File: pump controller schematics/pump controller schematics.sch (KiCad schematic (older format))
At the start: 16 parts, among them J1 Barrel_Jack, M1 370 pump, Q1 IRF64ON, SW1 SW_DIP_x01, U1 LM555

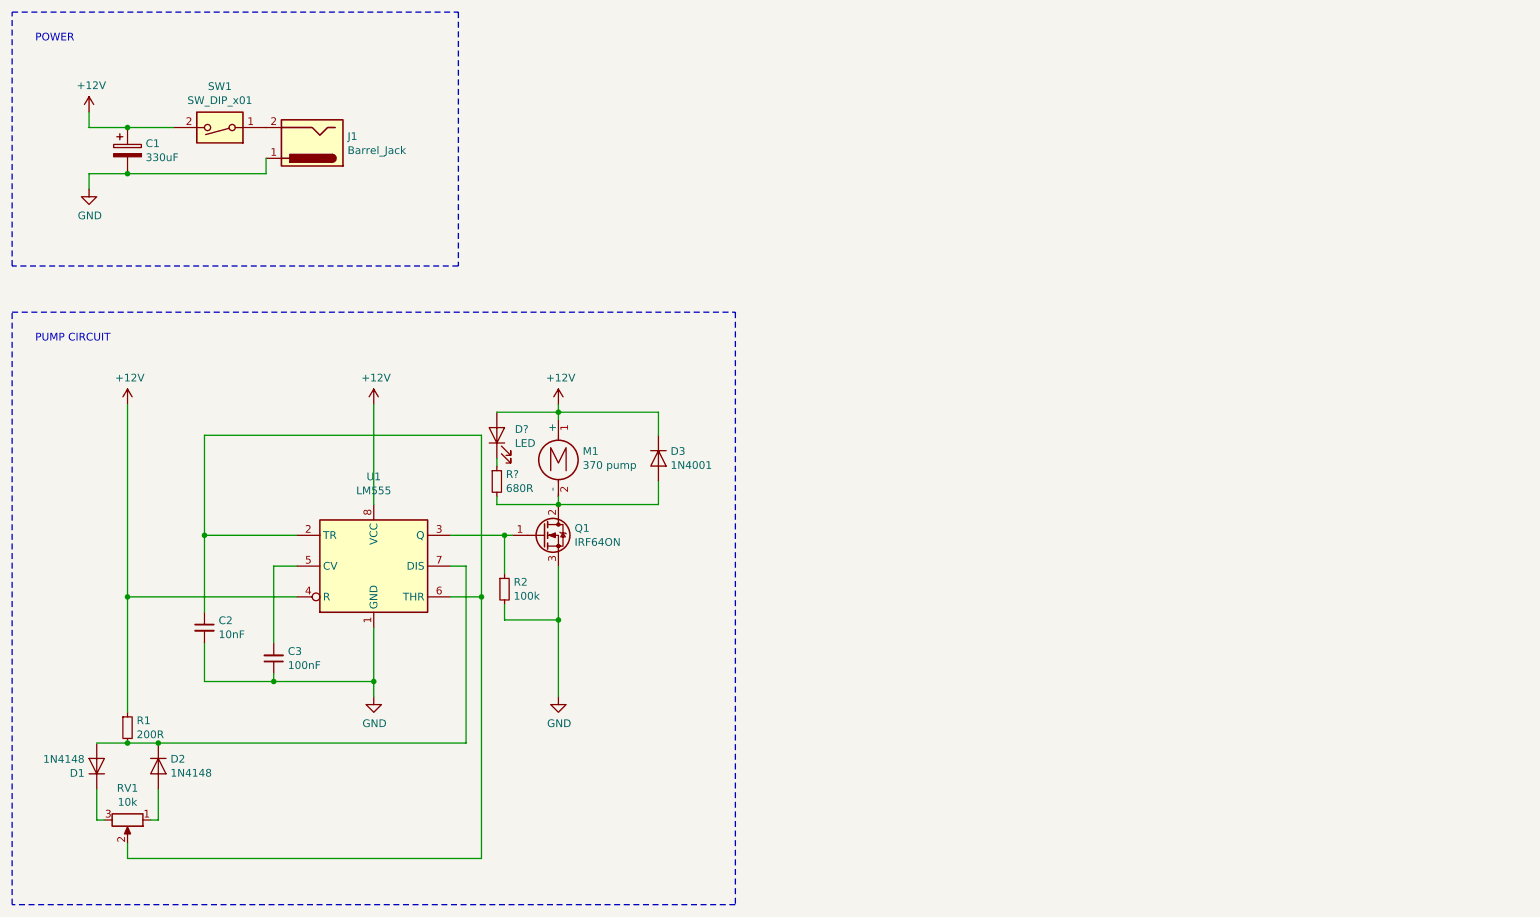
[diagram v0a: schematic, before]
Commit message: updated pump controller
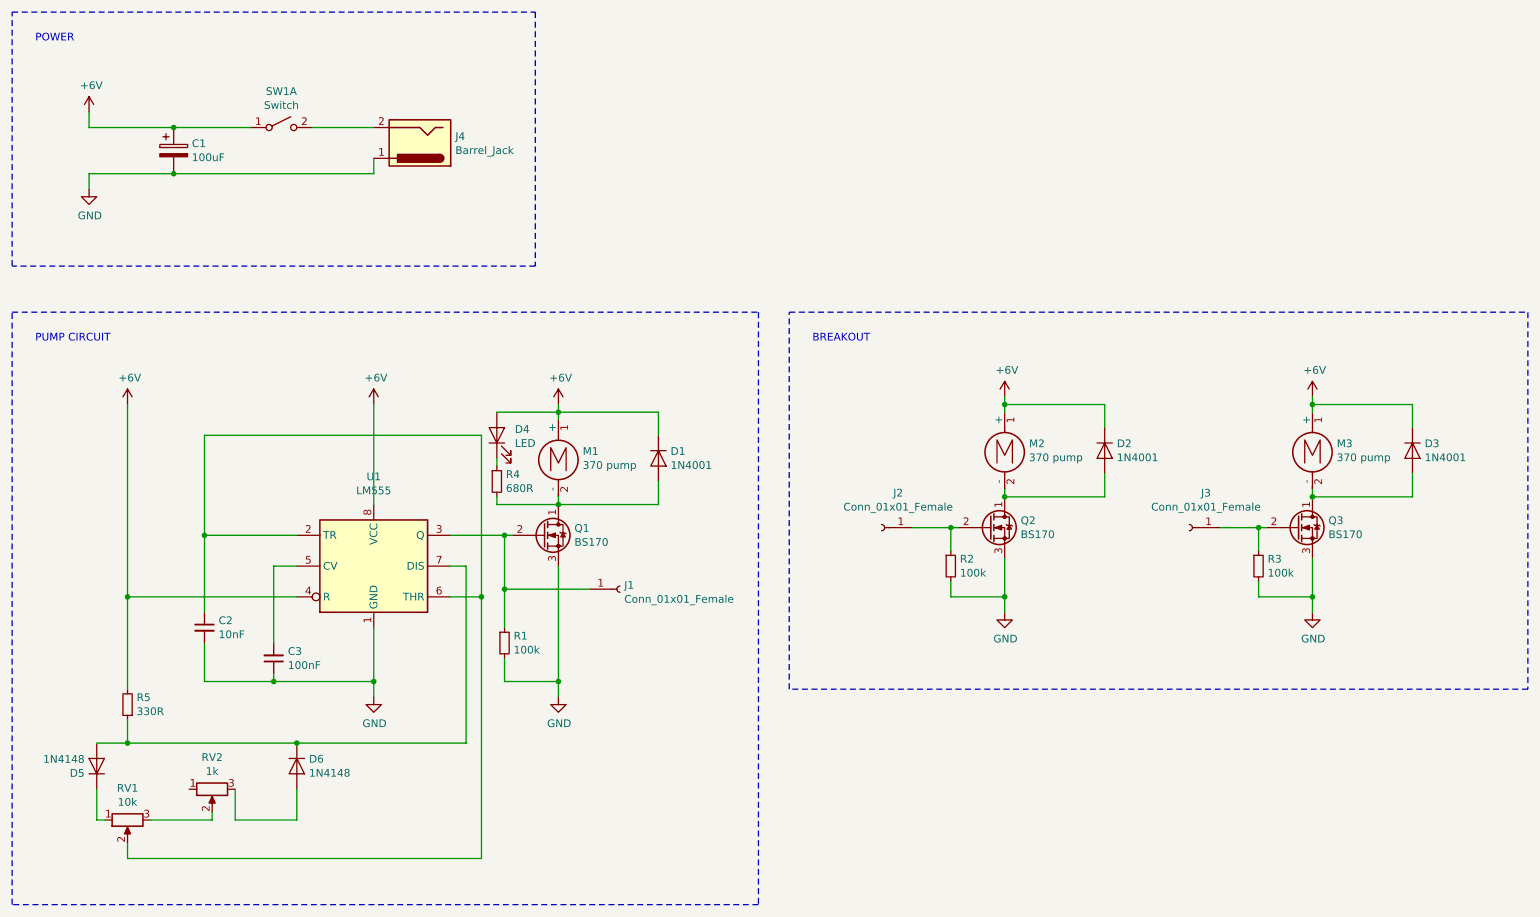
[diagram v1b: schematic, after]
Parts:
- removed Q1: IRF64ON, symbol Device:Q_NMOS_GDS
- removed R1: 200R, symbol Device:R_Small
- removed SW1: SW_DIP_x01, symbol Switch:SW_DIP_x01
- added D2, D3: 1N4001, Diode_THT:D_DO-41_SOD81_P10.16mm_Horizontal, symbol Diode:1N4001
- added J1, J2, J3: Conn_01x01_Female, Connector_PinHeader_2.54mm:PinHeader_1x01_P2.54mm_Vertical, symbol Connector:Conn_01x01_Female
- added M2, M3: 370 pump, Connector_PinHeader_2.54mm:PinHeader_1x03_P2.54mm_Vertical, symbol Motor:Motor_DC
- added Q1, Q2, Q3: BS170, Package_TO_SOT_THT:TO-92_Inline, symbol Transistor_FET:BS170
- added R2, R3: 100k, Resistor_THT:R_Axial_DIN0207_L6.3mm_D2.5mm_P7.62mm_Horizontal, symbol Device:R_Small
- added R5: 330R, Resistor_THT:R_Axial_DIN0207_L6.3mm_D2.5mm_P7.62mm_Horizontal, symbol Device:R_Small
- added RV2: 1k, Potentiometer_THT:Potentiometer_Runtron_RM-065_Vertical, symbol Device:R_POT
- added SW1: Switch, Connector_PinHeader_2.54mm:PinHeader_1x02_P2.54mm_Vertical, symbol Switch:SW_DPST_x2
- C1: value 330uF -> 100uF; footprint (none) -> Capacitor_THT:CP_Radial_D7.5mm_P2.50mm
- C2, C3: footprint (none) -> Capacitor_THT:C_Disc_D4.3mm_W1.9mm_P5.00mm
- D4: renamed from D?; footprint (none) -> LED_THT:LED_D3.0mm
- J4: renamed from J1; footprint (none) -> Connector_BarrelJack:BarrelJack_Horizontal
- M1, RV1: footprint (none) -> Connector_PinHeader_2.54mm:PinHeader_1x03_P2.54mm_Vertical
- R1: renamed from R2; footprint (none) -> Resistor_THT:R_Axial_DIN0207_L6.3mm_D2.5mm_P7.62mm_Horizontal
- R4: renamed from R?; footprint (none) -> Resistor_THT:R_Axial_DIN0207_L6.3mm_D2.5mm_P7.62mm_Horizontal
- U1: footprint (none) -> Package_DIP:DIP-8_W7.62mm_Socket_LongPads
- renumbered D3 to D1, D1 to D5, D2 to D6
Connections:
- net GND: now also Q1.3 (S), Q2.3 (S), Q3.3 (S), R2.2, R3.2
- net at J4.2: now also SW1.2 (B)
- net at R1.1, U1.3 (Q): now also J1.1 (Pin_1), Q1.2 (G)
- net at D5.2 (A), D6.1 (K), U1.7 (DIS): now also R5.1
- net at D6.2 (A): now also RV2.3; no longer RV1.1
- net at D5.1 (K): now also RV1.1; no longer RV1.3
- net at D1.2 (A), M1.2 (-), R4.2: now also Q1.1 (D)
- net +12V renamed +6V
- net +6V: now also D2.1 (K), D3.1 (K), M2.1 (+), M3.1 (+), R5.2, SW1.1 (A)
- new net: RV1.3, RV2.2
- new net: D2.2 (A), M2.2 (-), Q2.1 (D)
- new net: J2.1 (Pin_1), Q2.2 (G), R2.1
- new net: D3.2 (A), M3.2 (-), Q3.1 (D)
- new net: J3.1 (Pin_1), Q3.2 (G), R3.1
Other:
- note added: "BREAKOUT"
- moved on the sheet: C1, D6, J4, R1
